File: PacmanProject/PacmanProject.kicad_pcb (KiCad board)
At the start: 2 copper layers, 127 x 85 mm, 17 parts, among them J1 Conn_01x02, SW1 SW_Push, SW2 SW_Push, SW3 SW_Push, SW4 SW_Push, SW5 SW_Wuerth_450301014042, U1 Pico

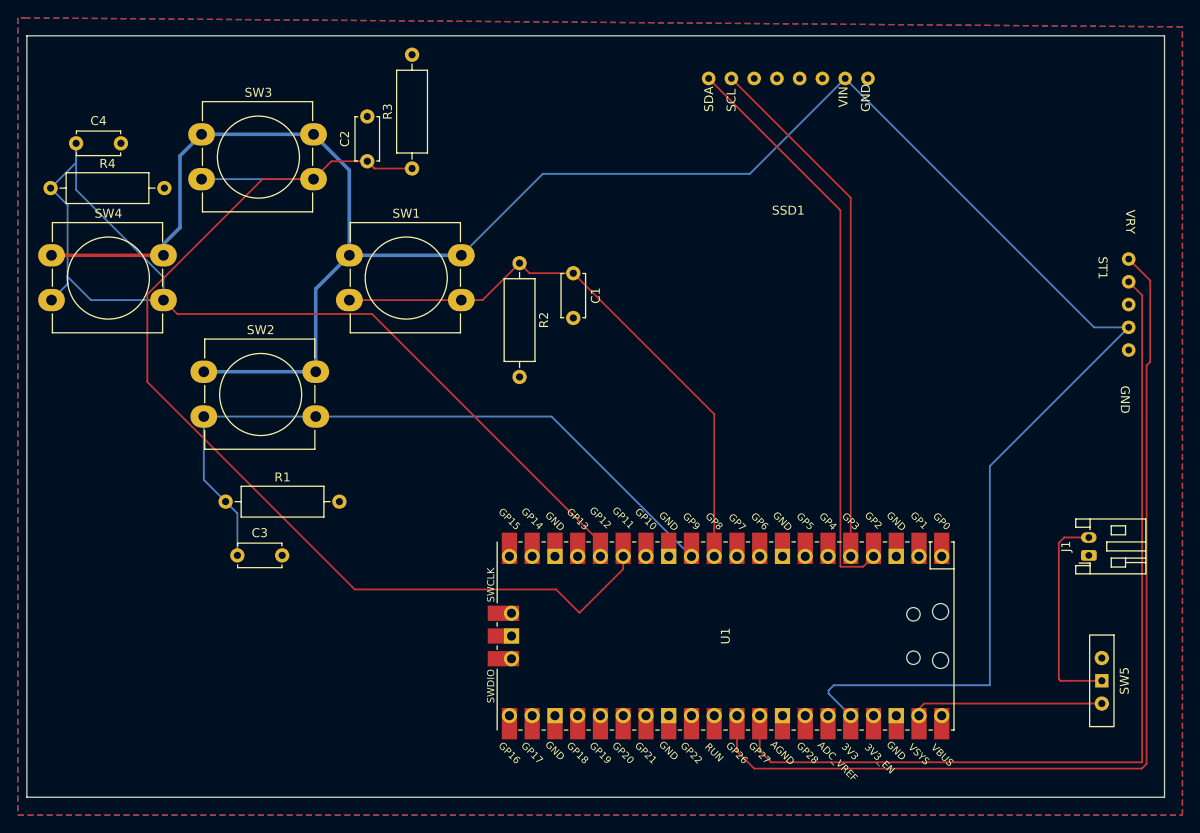
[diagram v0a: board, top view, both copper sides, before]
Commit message: Fixed the Connections to display on PCB
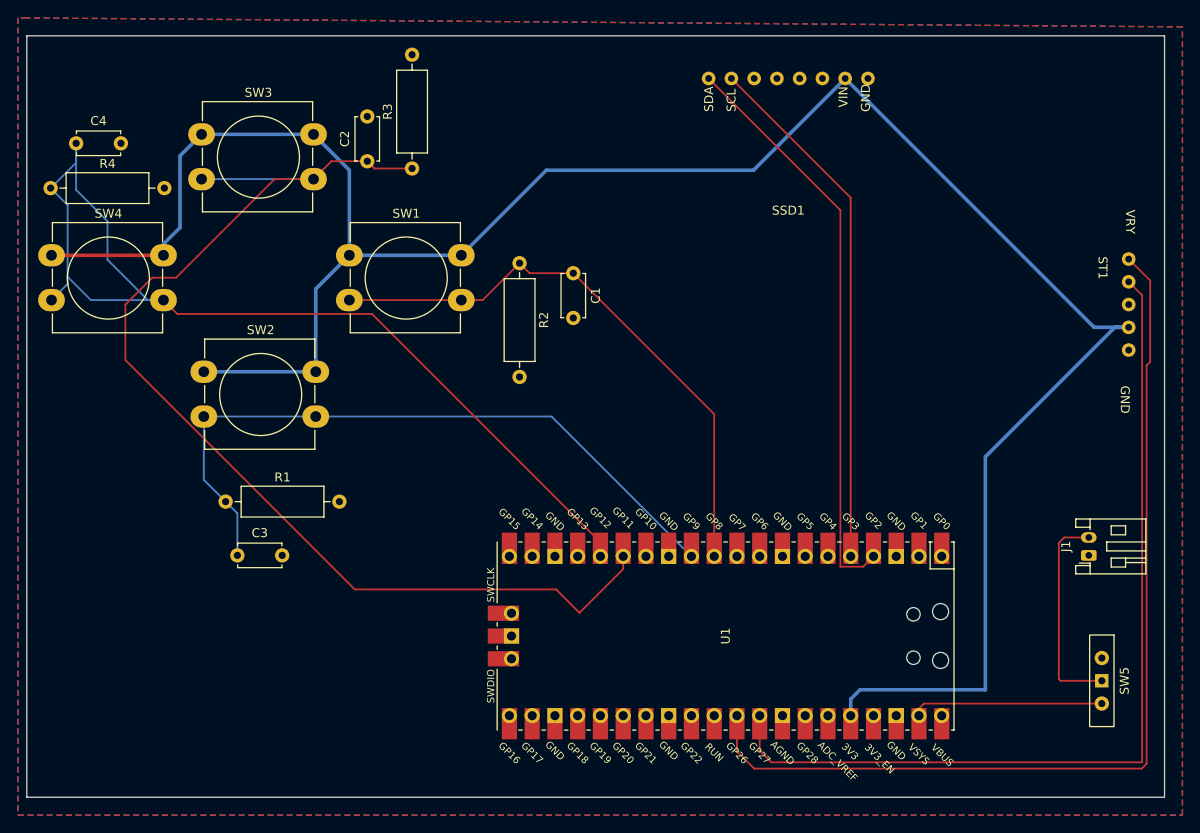
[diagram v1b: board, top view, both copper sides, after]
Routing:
- net +3.3V: track 257.8 -> 254.6 mm
- net /C: track 125.6 -> 128.4 mm
- net /D: track 115.1 -> 116.1 mm
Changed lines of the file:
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@@
 			(outputformat 1)
 			(mirror no)
-			(drillshape 1)
+			(drillshape 0)
 			(scaleselection 1)
-			(outputdirectory "")
+			(outputdirectory "PackmanGerbers/")
 		)
 	)
@@
 		(tags "tact sw push 12mm")
 		(property "Reference" "SW3"
-			(at 6.35 -4.66 360)
+			(at 6.35 -4.66 0)
 			(layer "F.SilkS")
 			(effects
@@
 		)
 		(property "Value" "SW_Push"
-			(at 6.35 9.93 360)
+			(at 6.35 9.93 0)
 			(layer "F.Fab")
 			(effects
@@
 		)
 		(fp_text user "${REFERENCE}"
-			(at 6.35 2.54 360)
+			(at 6.35 2.54 0)
 			(layer "F.Fab")
 			(effects
@@
 	)
 	(segment
-		(start 201.08 120.8)
-		(end 178.607969 120.8)
+		(start 156 86)
+		(end 158.653984 86)
 		(width 0.2)
 		(layer "F.Cu")
@@
 	)
 	(segment
-		(start 208.57 117.11)
-		(end 208.57 118.53)
+		(start 208.57 118.53)
+		(end 203.69 123.41)
 		(width 0.2)
 		(layer "F.Cu")
@@
 	)
 	(segment
-		(start 180.81 73.81)
-		(end 180 73)
+		(start 201.08 120.8)
+		(end 178.607969 120.8)
 		(width 0.2)
 		(layer "F.Cu")
@@
 	)
 	(segment
-		(start 155.45 87.857969)
-		(end 168.307969 75)
+		(start 180.81 73.81)
+		(end 180 73)
 		(width 0.2)
 		(layer "F.Cu")
@@
 	)
 	(segment
-		(start 168.307969 75)
-		(end 174 75)
+		(start 208.57 117.11)
+		(end 208.57 118.53)
 		(width 0.2)
 		(layer "F.Cu")
@@
 	)
 	(segment
-		(start 208.57 118.53)
-		(end 203.69 123.41)
+		(start 158.653984 86)
+		(end 169.653984 75)
 		(width 0.2)
 		(layer "F.Cu")
@@
 	(segment
 		(start 178.607969 120.8)
-		(end 155.45 97.642031)
+		(end 153 95.192031)
 		(width 0.2)
 		(layer "F.Cu")
@@
 	)
 	(segment
-		(start 203.69 123.41)
-		(end 201.08 120.8)
+		(start 153 95.192031)
+		(end 153 89)
 		(width 0.2)
 		(layer "F.Cu")
@@
 	)
 	(segment
-		(start 155.45 97.642031)
-		(end 155.45 87.857969)
+		(start 153 89)
+		(end 156 86)
+		(width 0.2)
+		(layer "F.Cu")
+		(net 3)
+	)
+	(segment
+		(start 203.69 123.41)
+		(end 201.08 120.8)
+		(width 0.2)
+		(layer "F.Cu")
+		(net 3)
+	)
+	(segment
+		(start 169.653984 75)
+		(end 174 75)
 		(width 0.2)
 		(layer "F.Cu")
@@
 	)
 	(segment
+		(start 151 79.692031)
+		(end 151 84)
+		(width 0.2)
+		(layer "B.Cu")
+		(net 5)
+	)
+	(segment
 		(start 157.25 88.5)
 		(end 149.15 88.5)
@@
 	)
 	(segment
-		(start 157.25 85.942031)
-		(end 157.25 88.5)
+		(start 147.5 76.192031)
+		(end 151 79.692031)
 		(width 0.2)
 		(layer "B.Cu")
@@
 	)
 	(segment
+		(start 151 84)
+		(end 155.5 88.5)
+		(width 0.2)
+		(layer "B.Cu")
+		(net 5)
+	)
+	(segment
+		(start 155.5 88.5)
+		(end 157.25 88.5)
+		(width 0.2)
+		(layer "B.Cu")
+		(net 5)
+	)
+	(segment
 		(start 146.55 86.7)
 		(end 144.75 88.5)
@@
 	)
 	(segment
-		(start 147.5 76.192031)
-		(end 157.25 85.942031)
-		(width 0.2)
-		(layer "B.Cu")
-		(net 5)
-	)
-	(segment
 		(start 257.2 115.6)
 		(end 257.8 115)
@@
 	)
 	(segment
-		(start 178 83.5)
-		(end 190.5 83.5)
+		(start 233.97 133.03)
+		(end 235 132)
 		(width 0.4)
 		(layer "B.Cu")
@@
 	)
 	(segment
-		(start 159.1 80.4)
-		(end 159.1 72.4)
+		(start 178 83.5)
+		(end 190.5 83.5)
 		(width 0.4)
 		(layer "B.Cu")
@@
 	)
 	(segment
-		(start 249.5 131.5)
-		(end 249.5 107.04)
-		(width 0.2)
-		(layer "B.Cu")
-		(net 10)
-	)
-	(segment
-		(start 222.71 74.4)
-		(end 233.35 63.76)
-		(width 0.2)
+		(start 159.1 80.4)
+		(end 159.1 72.4)
+		(width 0.4)
 		(layer "B.Cu")
 		(net 10)
 	)
 	(segment
-		(start 232.07 131.5)
-		(end 249.5 131.5)
-		(width 0.2)
+		(start 249 132)
+		(end 249 106)
+		(width 0.4)
 		(layer "B.Cu")
 		(net 10)
@@
 	)
 	(segment
-		(start 231.5 132.07)
-		(end 232.07 131.5)
-		(width 0.2)
-		(layer "B.Cu")
-		(net 10)
-	)
-	(segment
-		(start 233.97 134.89)
-		(end 231.5 132.42)
-		(width 0.2)
+		(start 223.11 74)
+		(end 233.35 63.76)
+		(width 0.4)
 		(layer "B.Cu")
 		(net 10)
@@
 	)
 	(segment
-		(start 233.35 63.76)
-		(end 261.13 91.54)
-		(width 0.2)
-		(layer "B.Cu")
-		(net 10)
-	)
-	(segment
-		(start 249.5 107.04)
-		(end 265 91.54)
-		(width 0.2)
+		(start 261.13 91.54)
+		(end 233.35 63.76)
+		(width 0.4)
 		(layer "B.Cu")
 		(net 10)
 	)
 	(segment
-		(start 231.5 132.42)
-		(end 231.5 132.07)
-		(width 0.2)
+		(start 190.5 83.5)
+		(end 200 74)
+		(width 0.4)
 		(layer "B.Cu")
 		(net 10)
 	)
 	(segment
-		(start 261.13 91.54)
+		(start 263.46 91.54)
 		(end 265 91.54)
-		(width 0.2)
+		(width 0.4)
 		(layer "B.Cu")
 		(net 10)
 	)
 	(segment
-		(start 199.6 74.4)
-		(end 222.71 74.4)
-		(width 0.2)
+		(start 233.97 134.89)
+		(end 233.97 133.03)
+		(width 0.4)
 		(layer "B.Cu")
 		(net 10)
 	)
 	(segment
-		(start 190.5 83.5)
-		(end 199.6 74.4)
-		(width 0.2)
+		(start 159.1 72.4)
+		(end 161.5 70)
+		(width 0.4)
 		(layer "B.Cu")
 		(net 10)
 	)
 	(segment
-		(start 159.1 72.4)
-		(end 161.5 70)
+		(start 265 91.54)
+		(end 261.13 91.54)
 		(width 0.4)
 		(layer "B.Cu")
@@
 		(width 0.4)
 		(layer "B.Cu")
+		(net 10)
+	)
+	(segment
+		(start 249 106)
+		(end 263.46 91.54)
+		(width 0.4)
+		(layer "B.Cu")
+		(net 10)
+	)
+	(segment
+		(start 235 132)
+		(end 249 132)
+		(width 0.4)
+		(layer "B.Cu")
+		(net 10)
+	)
+	(segment
+		(start 200 74)
+		(end 223.11 74)
+		(width 0.4)
+		(layer "B.Cu")

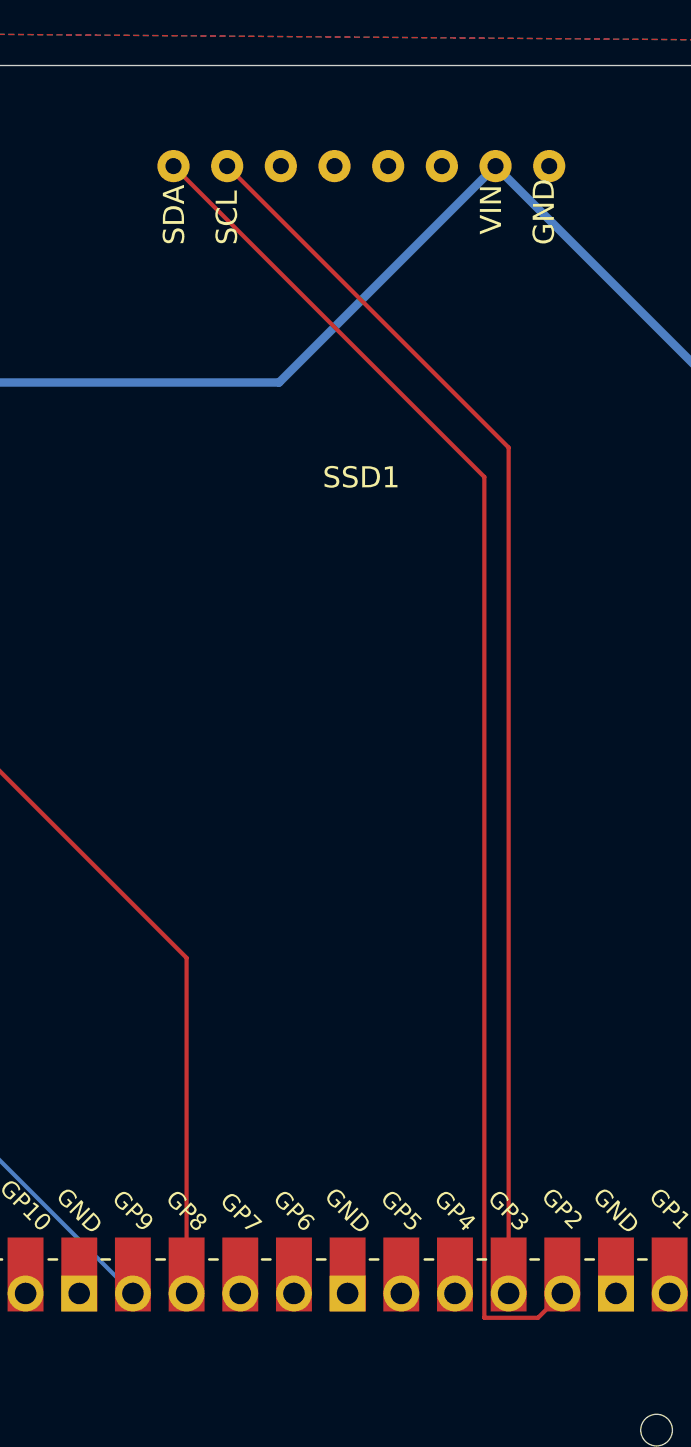
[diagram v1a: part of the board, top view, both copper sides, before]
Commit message: Fixed the Connections to display on PCB
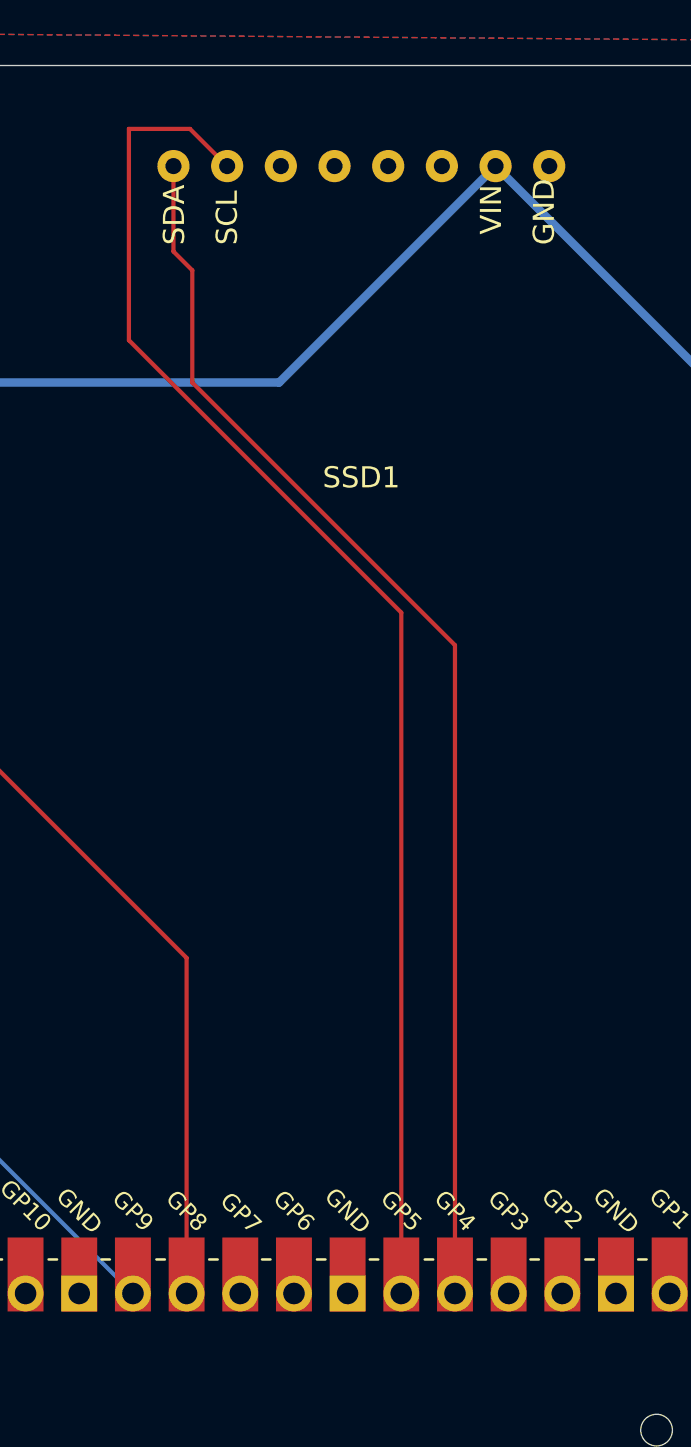
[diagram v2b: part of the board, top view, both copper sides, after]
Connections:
- SW5 pad 2: GND -> unconnected-(SW5-C-Pad2)
- U1 pad 4: /SDA -> unconnected-(U1-GPIO2-Pad4)
- U1 pad 5: /SCL -> unconnected-(U1-GPIO3-Pad5)
- U1 pad 6: unconnected-(U1-GPIO4-Pad6) -> /SDA
- U1 pad 7: unconnected-(U1-GPIO5-Pad7) -> /SCL
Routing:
- net /SCL: track 58.9 -> 65.8 mm
- net /SDA: track 64.8 -> 58.9 mm
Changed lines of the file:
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@@
 	(net 27 "unconnected-(U1-GPIO15-Pad20)_1")
 	(net 28 "unconnected-(U1-GPIO17-Pad22)_1")
-	(net 29 "unconnected-(U1-GPIO4-Pad6)")
+	(net 29 "unconnected-(SW5-C-Pad2)")
 	(net 30 "unconnected-(U1-GPIO21-Pad27)_1")
 	(net 31 "unconnected-(U1-GPIO18-Pad24)")
@@
 	(net 50 "unconnected-(U1-GPIO10-Pad14)")
 	(net 51 "unconnected-(U1-VBUS-Pad40)")
-	(net 52 "unconnected-(U1-GPIO5-Pad7)")
+	(net 52 "unconnected-(U1-GPIO3-Pad5)")
 	(net 53 "unconnected-(U1-GND-Pad3)_1")
 	(net 54 "unconnected-(U1-GND-Pad23)_1")
@@
 	(net 64 "unconnected-(U1-GPIO1-Pad2)_1")
 	(net 65 "unconnected-(U1-GPIO14-Pad19)_1")
-	(net 66 "unconnected-(U1-GPIO4-Pad6)_1")
+	(net 66 "unconnected-(U1-GPIO2-Pad4)")
 	(net 67 "unconnected-(U1-GPIO10-Pad14)_1")
 	(net 68 "unconnected-(U1-SWCLK-Pad41)_1")
@@
 	(net 75 "unconnected-(U1-GND-Pad8)_1")
 	(net 76 "unconnected-(U1-GPIO0-Pad1)_1")
-	(net 77 "unconnected-(U1-GPIO5-Pad7)_1")
+	(net 77 "unconnected-(U1-GPIO2-Pad4)_1")
 	(net 78 "unconnected-(U1-GND-Pad13)_1")
 	(net 79 "unconnected-(U1-ADC_VREF-Pad35)_1")
+	(net 80 "unconnected-(U1-GPIO3-Pad5)_1")
 	(footprint "Button_Switch_THT:SW_PUSH-12mm_Wuerth-430476085716"
 		(layer "F.Cu")
@@
 			(layers "*.Cu" "*.Mask")
 			(remove_unused_layers no)
-			(net 2 "GND")
+			(net 29 "unconnected-(SW5-C-Pad2)")
 			(pinfunction "C")
-			(pintype "passive")
+			(pintype "passive+no_connect")
 		)
 		(pad "3" thru_hole circle
@@
 			(layers "*.Cu" "*.Mask")
 			(remove_unused_layers no)
-			(net 11 "/SDA")
+			(net 77 "unconnected-(U1-GPIO2-Pad4)_1")
 			(pinfunction "GPIO2")
-			(pintype "bidirectional")
+			(pintype "bidirectional+no_connect")
 		)
 		(pad "4" smd rect
@@
 			)
 			(layers "F.Cu" "F.Mask")
-			(net 11 "/SDA")
+			(net 66 "unconnected-(U1-GPIO2-Pad4)")
 			(pinfunction "GPIO2")
-			(pintype "bidirectional")
+			(pintype "bidirectional+no_connect")
 		)
 		(pad "5" thru_hole oval
@@
 			(layers "*.Cu" "*.Mask")
 			(remove_unused_layers no)
-			(net 9 "/SCL")
+			(net 80 "unconnected-(U1-GPIO3-Pad5)_1")
 			(pinfunction "GPIO3")
-			(pintype "bidirectional")
+			(pintype "bidirectional+no_connect")
 		)
 		(pad "5" smd rect
@@
 			)
 			(layers "F.Cu" "F.Mask")
-			(net 9 "/SCL")
+			(net 52 "unconnected-(U1-GPIO3-Pad5)")
 			(pinfunction "GPIO3")
-			(pintype "bidirectional")
+			(pintype "bidirectional+no_connect")
 		)
 		(pad "6" thru_hole oval
@@
 			(layers "*.Cu" "*.Mask")
 			(remove_unused_layers no)
-			(net 66 "unconnected-(U1-GPIO4-Pad6)_1")
+			(net 11 "/SDA")
 			(pinfunction "GPIO4")
-			(pintype "bidirectional+no_connect")
+			(pintype "bidirectional")
 		)
 		(pad "6" smd rect
@@
 			)
 			(layers "F.Cu" "F.Mask")
-			(net 29 "unconnected-(U1-GPIO4-Pad6)")
+			(net 11 "/SDA")
 			(pinfunction "GPIO4")
-			(pintype "bidirectional+no_connect")
+			(pintype "bidirectional")
 		)
 		(pad "7" thru_hole oval
@@
 			(layers "*.Cu" "*.Mask")
 			(remove_unused_layers no)
-			(net 77 "unconnected-(U1-GPIO5-Pad7)_1")
+			(net 9 "/SCL")
 			(pinfunction "GPIO5")
-			(pintype "bidirectional+no_connect")
+			(pintype "bidirectional")
 		)
 		(pad "7" smd rect
@@
 			)
 			(layers "F.Cu" "F.Mask")
-			(net 52 "unconnected-(U1-GPIO5-Pad7)")
+			(net 9 "/SCL")
 			(pinfunction "GPIO5")
-			(pintype "bidirectional+no_connect")
+			(pintype "bidirectional")
 		)
 		(pad "8" thru_hole rect
@@
 	)
 	(segment
-		(start 233.97 77.08)
+		(start 216 72)
+		(end 216 62)
+		(width 0.2)
+		(layer "F.Cu")
+		(net 9)
+	)
+	(segment
+		(start 228.89 84.89)
+		(end 216 72)
+		(width 0.2)
+		(layer "F.Cu")
+		(net 9)
+	)
+	(segment
+		(start 216 62)
+		(end 218.89 62)
+		(width 0.2)
+		(layer "F.Cu")
+		(net 9)
+	)
+	(segment
+		(start 218.89 62)
 		(end 220.65 63.76)
 		(width 0.2)
@@
 	)
 	(segment
-		(start 233.97 117.11)
-		(end 233.97 77.08)
+		(start 228.89 117.11)
+		(end 228.89 84.89)
 		(width 0.2)
 		(layer "F.Cu")
@@
 	)
 	(segment
-		(start 236.51 117.11)
-		(end 235.36 118.26)
+		(start 218.11 67.801895)
+		(end 218.11 63.76)
+		(width 0.2)
+		(layer "F.Cu")
+		(net 11)
+	)
+	(segment
+		(start 219 68.691895)
+		(end 218.11 67.801895)
 		(width 0.2)
 		(layer "F.Cu")
@@
 	)
 	(segment
-		(start 232.82 118.26)
-		(end 232.82 78.47)
+		(start 231.43 86.43)
+		(end 219 74)
 		(width 0.2)
 		(layer "F.Cu")
@@
 	)
 	(segment
-		(start 232.82 78.47)
-		(end 218.11 63.76)
+		(start 219 74)
+		(end 219 68.691895)
 		(width 0.2)
 		(layer "F.Cu")
@@
 	)
 	(segment
-		(start 235.36 118.26)
-		(end 232.82 118.26)
+		(start 231.43 117.11)
+		(end 231.43 86.43)
 		(width 0.2)
 		(layer "F.Cu")
